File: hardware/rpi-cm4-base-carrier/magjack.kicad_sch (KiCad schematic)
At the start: 13 parts, among them J5 THD-02-R, J6 JT4-1202HL

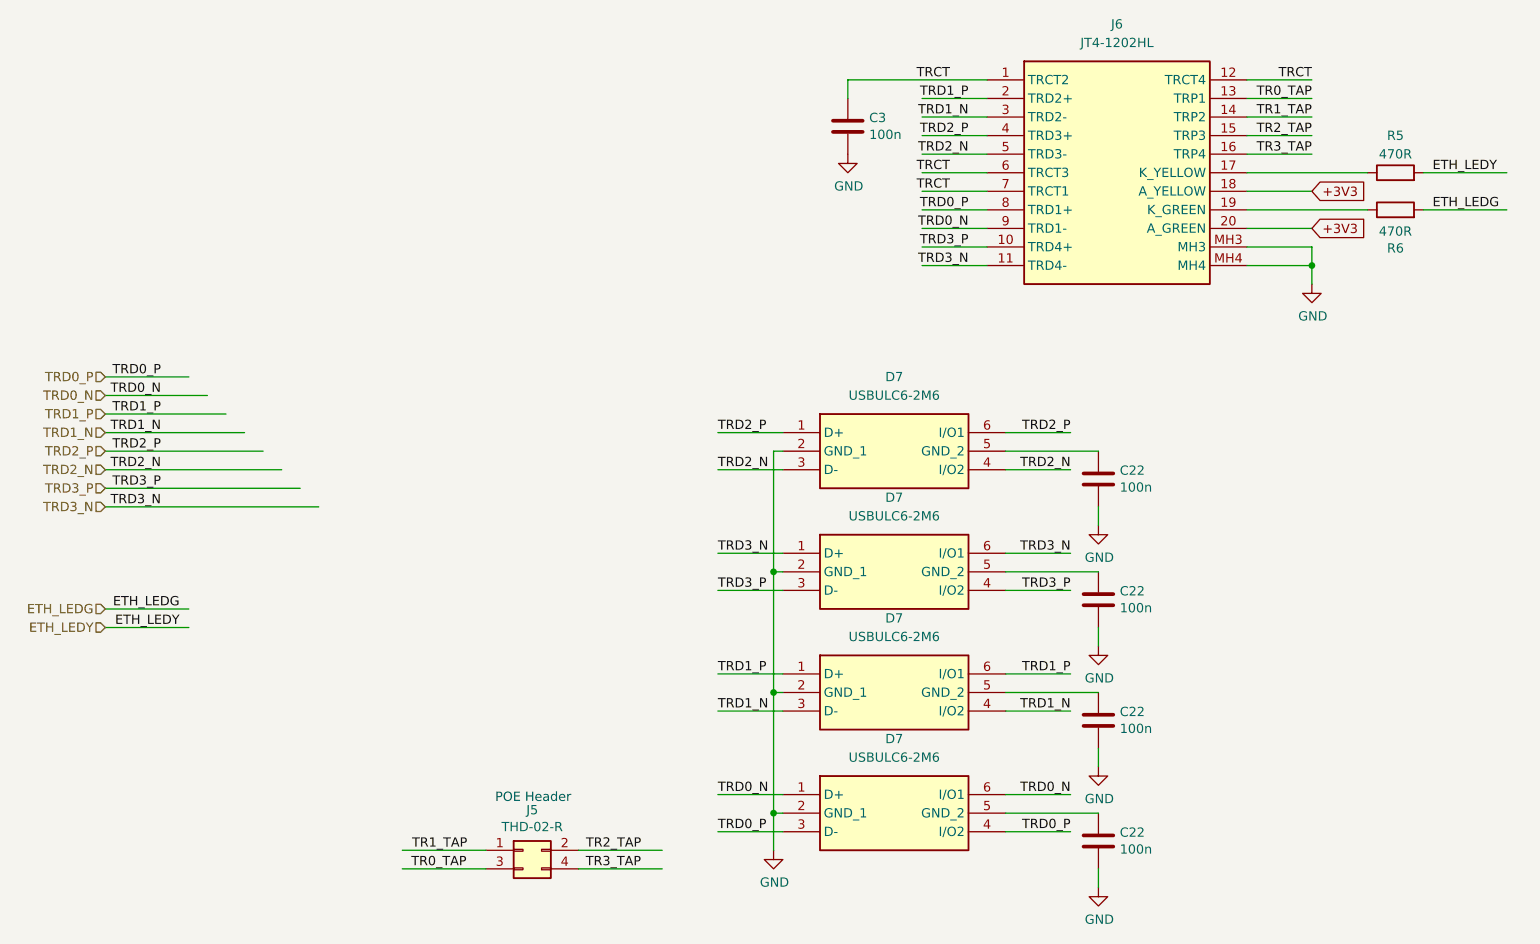
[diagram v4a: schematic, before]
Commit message: convert IC refs to U refs and re-annotate, add fiducials and extra via stitching to layout
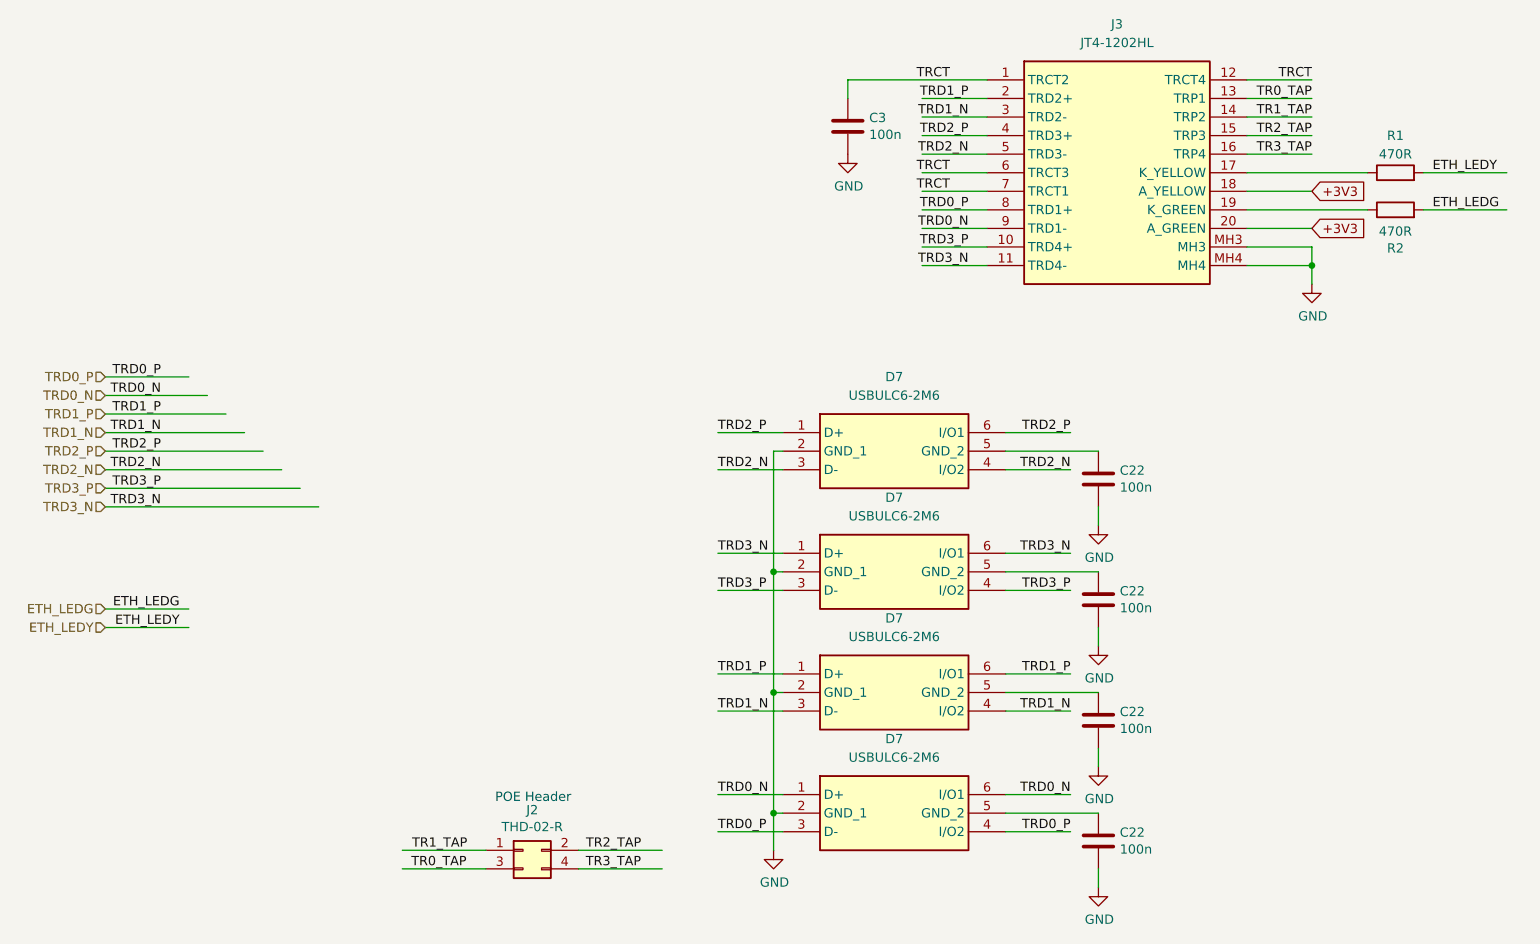
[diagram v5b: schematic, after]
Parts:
- renumbered J5 to J2, J6 to J3, R5 to R1, R6 to R2

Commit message: design files exported ready for manufacture, LCSC part numbers added throughout the library
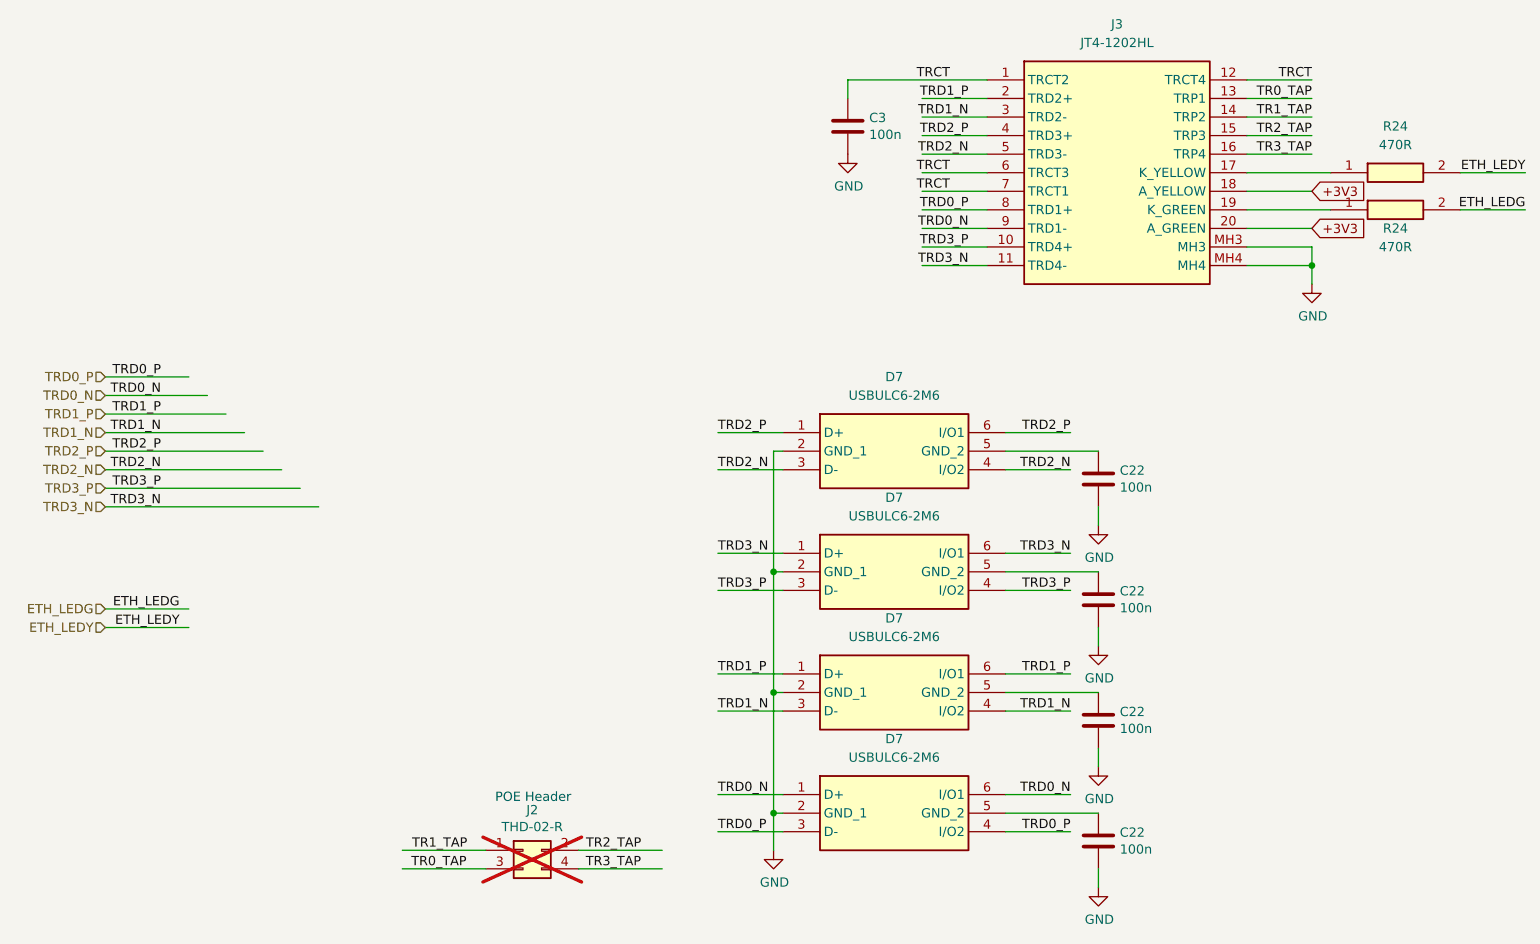
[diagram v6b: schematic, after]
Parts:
- removed R1, R2: 470R, Resistor_SMD:R_0402_1005Metric, symbol Device:R
- added R24 (x2): 470R, SamacSys_Parts:RESC1005X40N, symbol SamacSys_Parts:CR0402-JW-471GLF
- C22, C3: LCSC Part # (none) -> C152724; LCSC Part Number (none) -> C152724
- D7: LCSC Part # (none) -> C672213; LCSC Part Number (none) -> C672213
- J2: LCSC Part # (none) -> NF; LCSC Part Number (none) -> NF; now not fitted
- J3: LCSC Part # (none) -> C7212687; LCSC Part Number (none) -> C7212687
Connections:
- net ETH_LEDG: now also R24.2
- net ETH_LEDY: now also R24.2
- net at J3.17 (K_YELLOW): now also R24.1
- net at J3.19 (K_GREEN): now also R24.1
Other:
- title: (none) -> Raspberry Pi Compute Module 4 Control Node
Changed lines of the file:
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@@
 (kicad_sch (version 20230121) (generator eeschema)
   (paper "A4")
+  (title_block
+    (title "Raspberry Pi Compute Module 4 Control Node")
+    (date "2024-02-04")
+    (comment 2 "creativecommons.org/licenses/by-sa/4.0/")
+    (comment 3 "License: CC BY-SA 4.0")
+    (comment 4 "Author: Sam Earnshaw")
+  )
